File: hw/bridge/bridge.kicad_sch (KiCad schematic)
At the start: 37 parts, among them J1 USB_C_Receptacle_USB2.0_14P, J2 USB_C_Receptacle_USB2.0_14P, J3 DB9, U1 CH340E, U2 MAX485E, U3 74LVC2G240

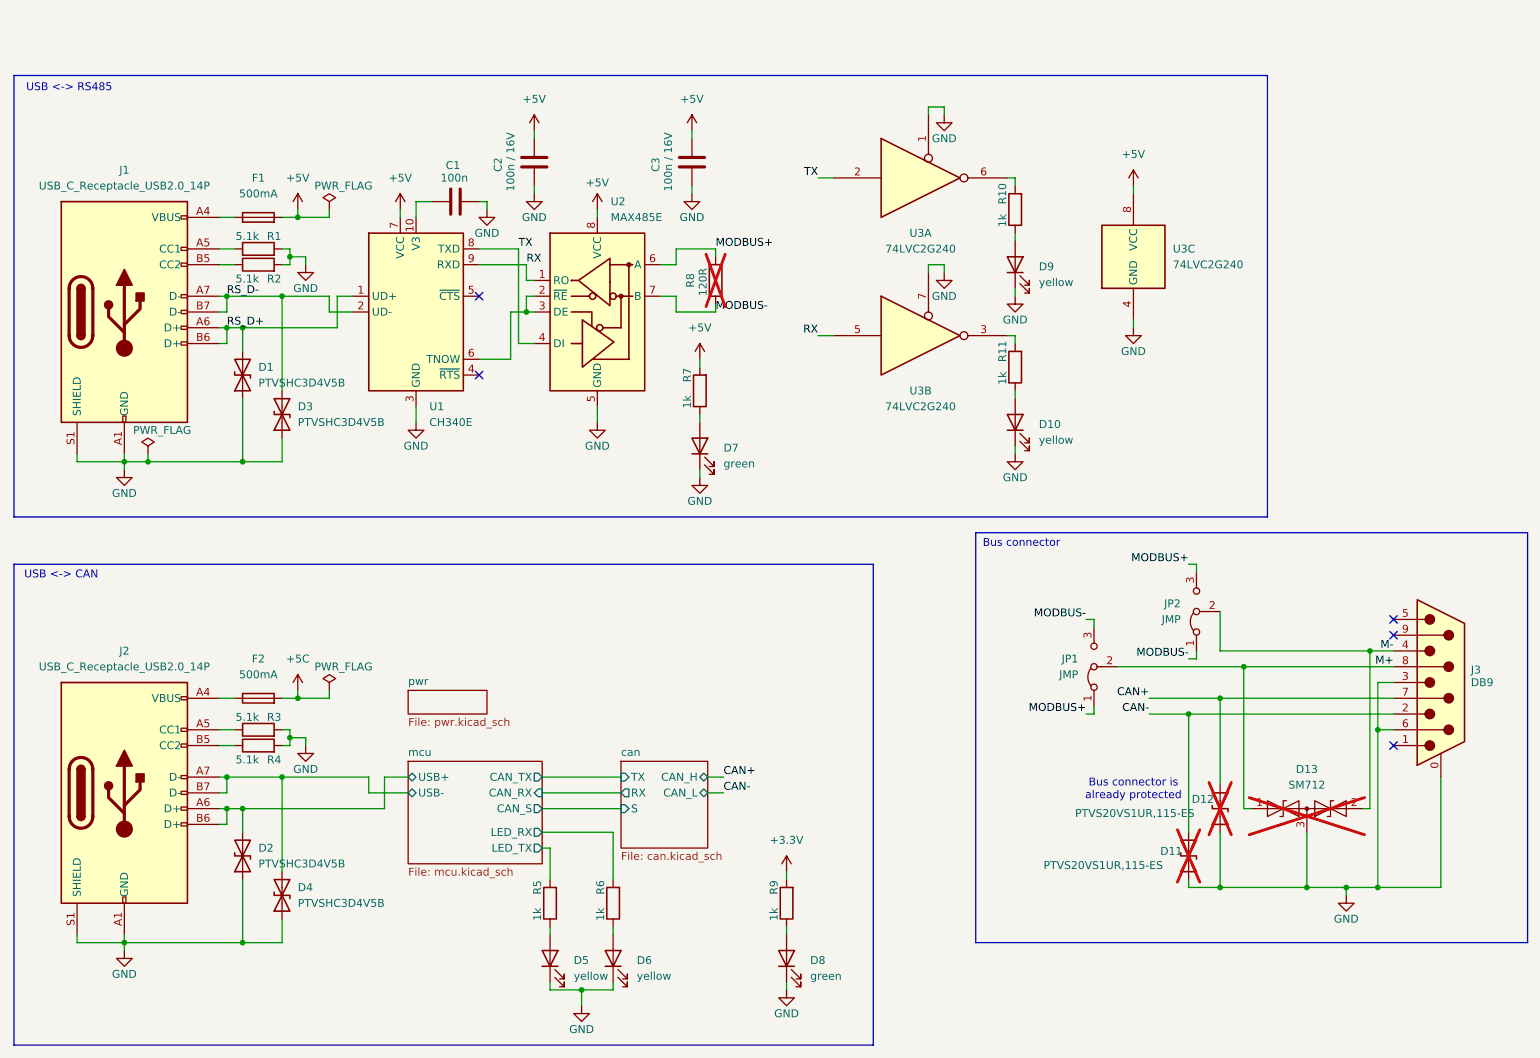
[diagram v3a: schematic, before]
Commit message: Redesign the PCB, remove DNP components
Signed-off-by: Mateusz Pająk <22417805+Tai-Min@users.noreply.github.com>
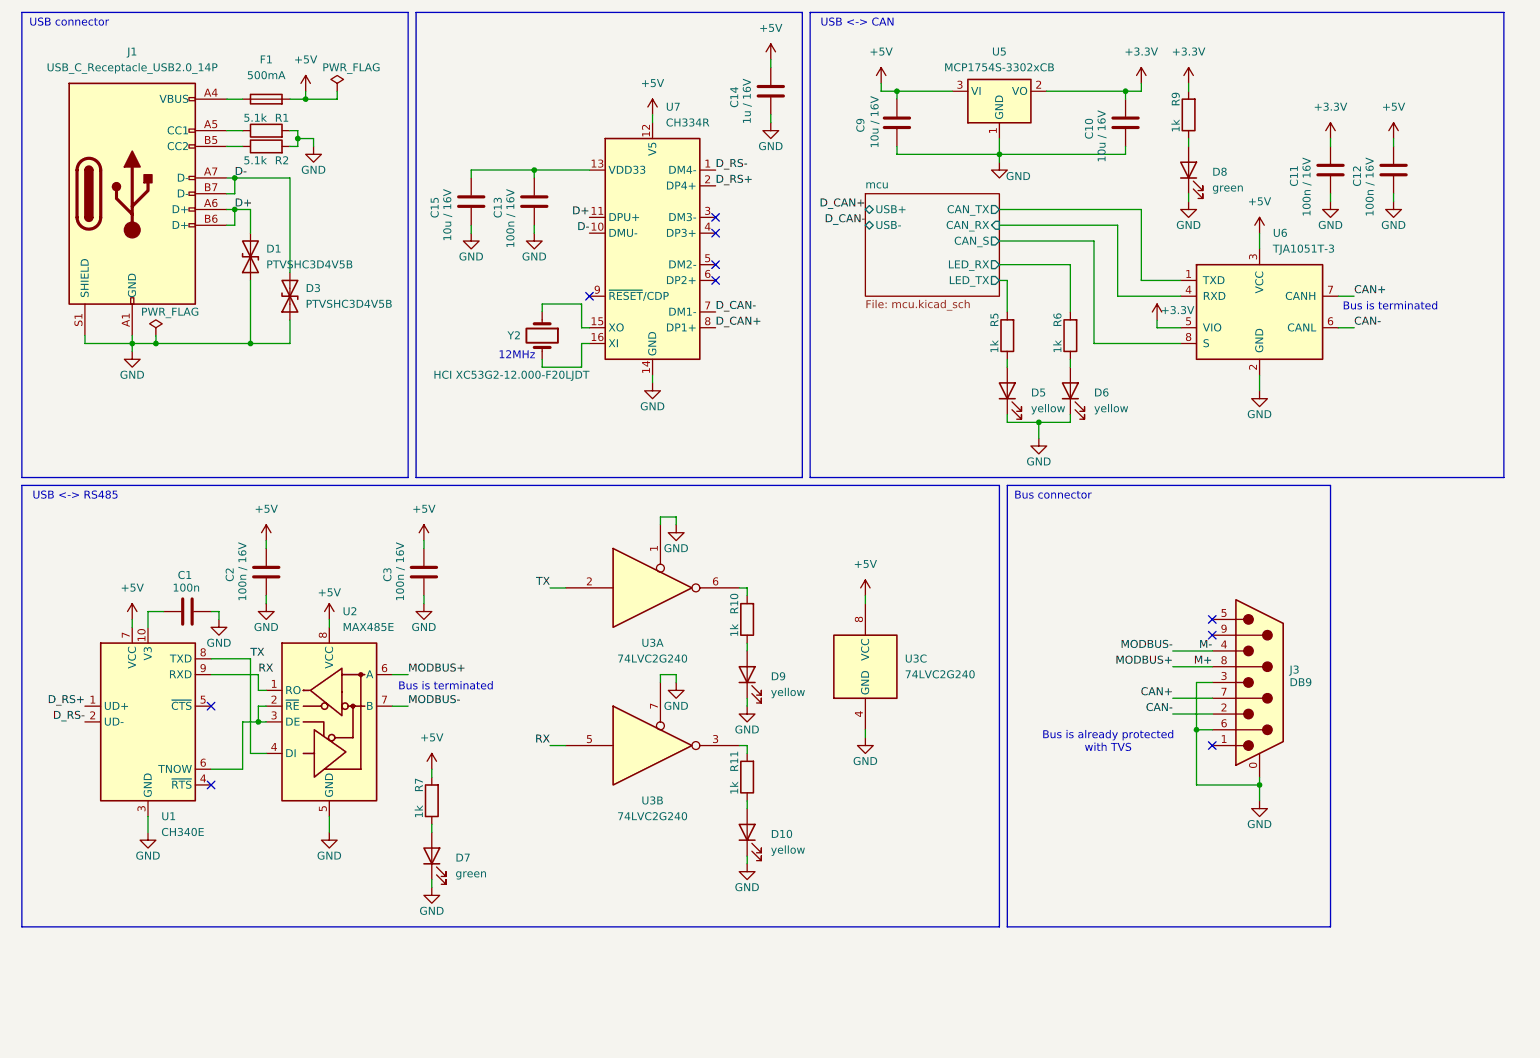
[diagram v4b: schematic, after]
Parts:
- removed D11, D12: PTVS20VS1UR,115-ES, Diode_SMD:D_SOD-123F, symbol Device:D_TVS
- removed D13: SM712, Package_TO_SOT_SMD:SOT-23, symbol Diode:SM712_SOT23
- removed D2, D4: PTVSHC3D4V5B, Diode_SMD:D_SOD-323, symbol Device:D_TVS
- removed F2: 500mA, Fuse:Fuse_1206_3216Metric, symbol Device:Fuse
- removed J2: USB_C_Receptacle_USB2.0_14P, Connector_USB:USB_C_Receptacle_Amphenol_12401610E4-2A_CircularHoles, symbol Connector:USB_C_Receptacle_USB2.0_14P
- removed JP1, JP2: JMP, Jumper:SolderJumper-3_P1.3mm_Bridged2Bar12_RoundedPad1.0x1.5mm, symbol Jumper:Jumper_3_Bridged12
- removed R3, R4: 5.1k, Resistor_SMD:R_1206_3216Metric, symbol Device:R
- removed R8: 120R, Resistor_SMD:R_1206_3216Metric, symbol Device:R
- added C10, C15, C9: 10u / 16V, Capacitor_SMD:C_0603_1608Metric, symbol Device:C
- added C11, C12, C13: 100n / 16V, Capacitor_SMD:C_0603_1608Metric, symbol Device:C
- added C14: 1u / 16V, Capacitor_SMD:C_0603_1608Metric, symbol Device:C
- added U5: MCP1754S-3302xCB, Package_TO_SOT_SMD:SOT-23, symbol Regulator_Linear:MCP1754S-3302xCB
- added U6: TJA1051T-3, Package_SO:SOIC-8_3.9x4.9mm_P1.27mm, symbol Interface_CAN_LIN:TJA1051T-3
- added U7: CH334R, Package_SO:QSOP-16_3.9x4.9mm_P0.635mm, symbol Interface_USB:CH334R
- added Y2: HCI XC53G2-12.000-F20LJDT, Crystal:Crystal_SMD_5032-2Pin_5.0x3.2mm, symbol Device:Crystal
- C1, C2, C3: footprint Capacitor_SMD:C_1206_3216Metric -> Capacitor_SMD:C_0603_1608Metric
- D10, D5, D6, D7, D8, D9: footprint LED_SMD:LED_1206_3216Metric -> LED_SMD:LED_0603_1608Metric
- F1: footprint Fuse:Fuse_1206_3216Metric -> Fuse:Fuse_0603_1608Metric
- R1, R10, R11, R2, R5, R6, R7, R9: footprint Resistor_SMD:R_1206_3216Metric -> Resistor_SMD:R_0603_1608Metric
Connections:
- net MODBUS+ is gone; now on net M+: U2.6 (A)
- net MODBUS- is gone; now on net M-: U2.7 (B)
- net +3.3V: now also C10.2, C11.2, U5.2 (VO), U6.5 (VIO)
- net +5V: now also C12.2, C14.2, C9.2, U5.3 (VI), U6.3 (VCC), U7.12 (V5)
- net CAN+: now also U6.7 (CANH)
- net CAN-: now also U6.6 (CANL)
- net GND: now also C10.1, C11.1, C12.1, C13.1, C14.1, C15.1, C9.1, U5.1 (GND), U6.2 (GND), U7.14 (GND)
- net RS_D+ renamed D+
- net D+: now also U7.11 (DPU+); no longer U1.1 (UD+)
- net RS_D- renamed D-
- net D-: now also U7.10 (DMU-); no longer U1.2 (UD-)
- new net: C13.2, C15.2, U7.13 (VDD33)
- new net: U7.15 (XO), Y2.1
- new net: U7.16 (XI), Y2.2
- new net D_CAN+: U7.8 (DP1+)
- new net D_CAN-: U7.7 (DM1-)
- new net D_RS+: U1.1 (UD+), U7.2 (DP4+)
- new net D_RS-: U1.2 (UD-), U7.1 (DM4-)
- new net mcu/CAN_RX: U6.4 (RXD)
- new net mcu/CAN_S: U6.8 (S)
- new net mcu/CAN_TX: U6.1 (TXD)
- no-connect marks 5 -> 10
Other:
- removed sheet can
- removed sheet pwr
- note added: "12MHz"
- note added: "Bus is already protected with TVS"
- note added: "Bus is terminated"
- note added: "USB connector"
- note removed: "Bus connector is already protected"
- moved on the sheet: C1, C2, C3, D1, D10, D3, D5, D6, D7, D8, D9, F1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

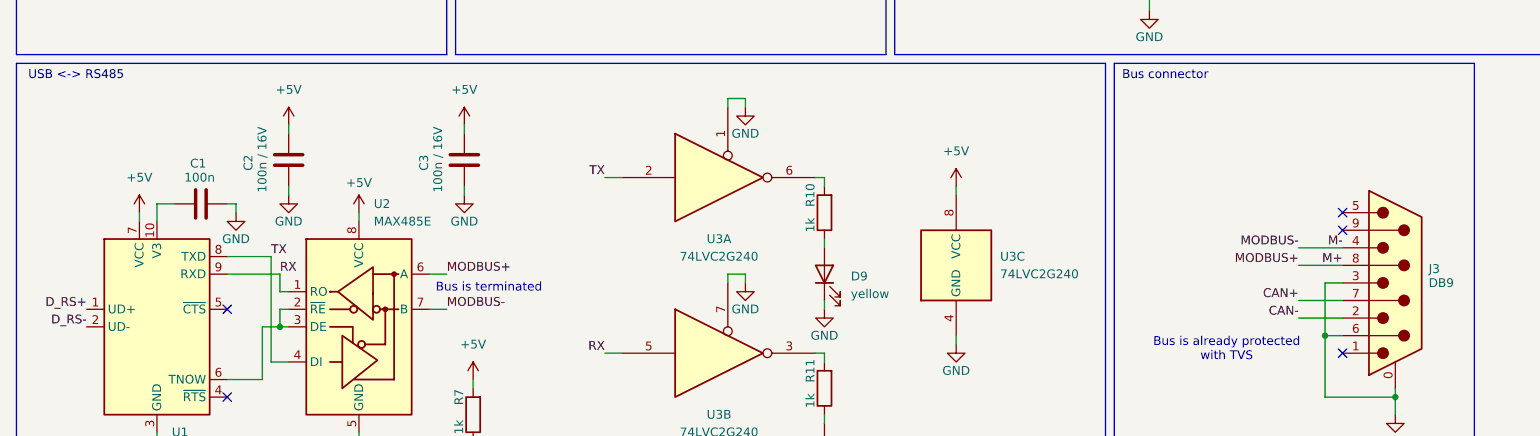
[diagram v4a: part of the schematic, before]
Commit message: Add datasheets, add BOM links
Signed-off-by: Mateusz Pająk <22417805+Tai-Min@users.noreply.github.com>
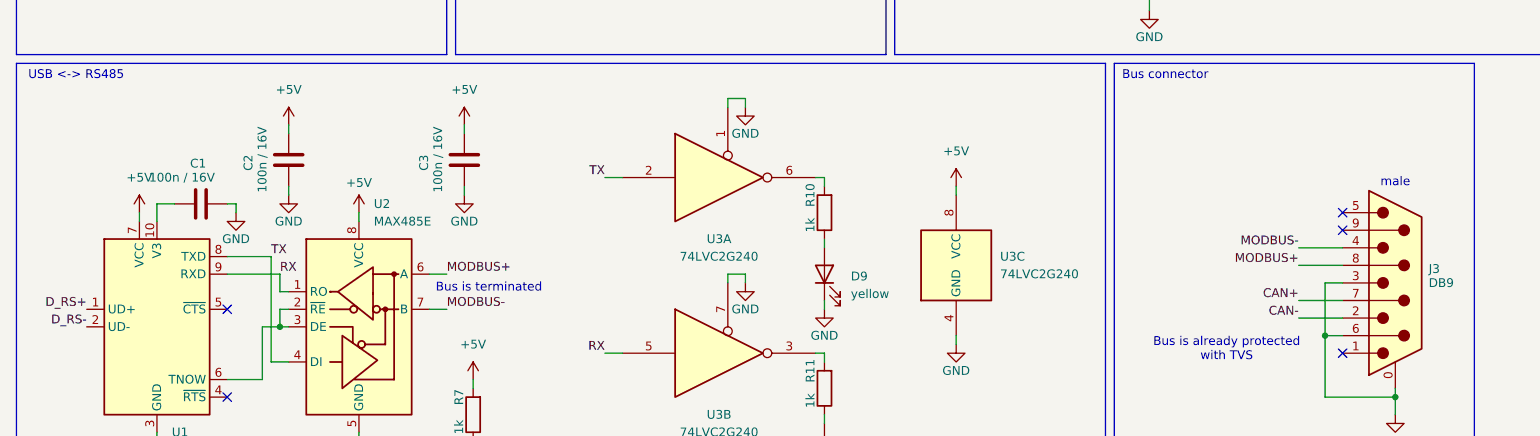
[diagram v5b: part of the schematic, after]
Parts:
- C1: value 100n -> 100n / 16V; LCSC (none) -> https://www.lcsc.com/product-detail/C66501.html
- C10, C15, C9: LCSC (none) -> https://www.lcsc.com/product-detail/C92487.html
- C11, C12, C13, C2, C3: LCSC (none) -> https://www.lcsc.com/product-detail/C66501.html
- C14: LCSC (none) -> https://www.lcsc.com/product-detail/C1592.html
- D1, D3: LCSC (none) -> https://www.lcsc.com/product-detail/C110752.html?s_z=n_PTVS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
- D10, D5, D6, D9: LCSC (none) -> https://www.lcsc.com/product-detail/C72038.html
- D7, D8: LCSC (none) -> https://www.lcsc.com/product-detail/C22371297.html
- F1: LCSC (none) -> https://www.lcsc.com/product-detail/C41380225.html
- J1: LCSC (none) -> https://www.lcsc.com/product-detail/C5119948.html?s_z=n_124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
- J3: LCSC (none) -> https://www.lcsc.com/product-detail/C19077344.html?s_z=n_ds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
- R1, R2: LCSC (none) -> https://www.lcsc.com/product-detail/C2907044.html
- R10, R11, R5, R6, R7, R9: LCSC (none) -> https://www.lcsc.com/product-detail/C22548.html
- U1: LCSC (none) -> https://www.lcsc.com/product-detail/C99652.html?s_z=n_ch340e
- U2: LCSC (none) -> https://www.lcsc.com/product-detail/C481667.html?s_z=n_max4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
- U3: LCSC (none) -> https://www.lcsc.com/product-detail/C730238.html?s_z=n_74LV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
- U5: LCSC (none) -> https://www.lcsc.com/product-detail/C625392.html?s_z=n_MCP1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
- U6: LCSC (none) -> https://www.lcsc.com/product-detail/C51954344.html?s_z=n_TJ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
- U7: LCSC (none) -> https://www.lcsc.com/product-detail/C4154405.html?s_z=n_ch3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
- Y2: LCSC (none) -> https://www.lcsc.com/product-detail/C2842275.html?s_z=n_HCI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
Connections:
- net M+ renamed MODBUS+
- net M- renamed MODBUS-
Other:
- note added: "male"

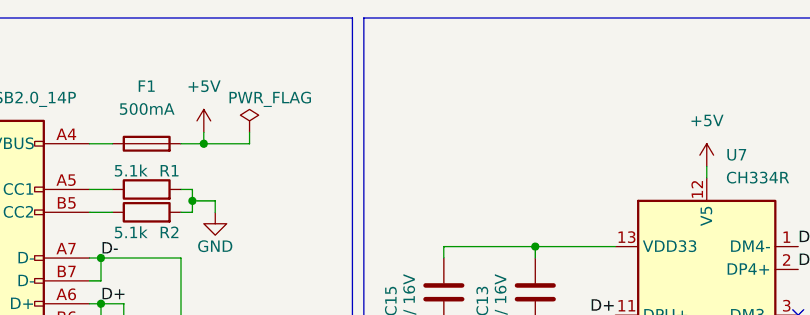
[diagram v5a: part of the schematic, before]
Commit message: Fix missing schematic header
Signed-off-by: Mateusz Pająk <22417805+Tai-Min@users.noreply.github.com>
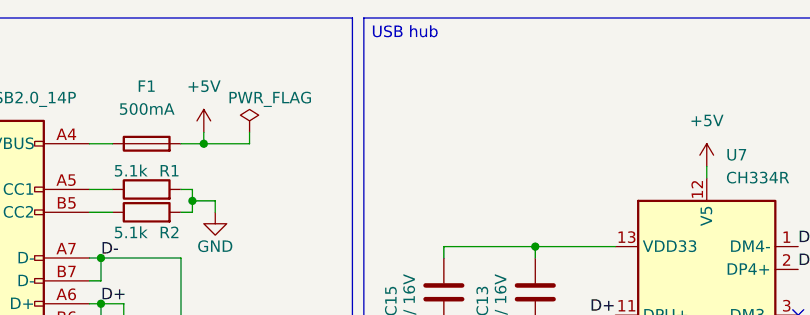
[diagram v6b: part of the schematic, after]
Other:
- note added: "USB hub"
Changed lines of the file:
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@@
+		)
+	)
+	(text "USB hub"
+		(exclude_from_sim no)
+		(at 97.282 15.748 0)
+		(effects
+			(font
+				(size 1.27 1.27)
+			)
 		)
 	)

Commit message: Minor fixes
Signed-off-by: Mateusz Pająk <22417805+Tai-Min@users.noreply.github.com>
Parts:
- removed U3: 74LVC2G240, Package_SO:TSSOP-8_3x3mm_P0.65mm, symbol 74xGxx:74LVC2G240
- added C4: 1u, Capacitor_SMD:C_0603_1608Metric, symbol Device:C
- added R12, R13, R14, R15: 0, Resistor_SMD:R_0603_1608Metric, symbol Device:R
- added R3, R4: 10k, Resistor_SMD:R_0603_1608Metric, symbol Device:R
- added U4: 74LVC2G04, Package_TO_SOT_SMD:SOT-23-6, symbol 74xGxx:74LVC2G04
- C1: renamed from C2; value 100n / 16V -> 100n
- C10: renamed from C11; value 100n / 16V -> 100n
- C11: renamed from C12; value 100n / 16V -> 100n
- C2: renamed from C1; value 100n / 16V -> 100n
- C3: value 100n / 16V -> 100n
- C5: renamed from C15; value 10u / 16V -> 10u
- C6: renamed from C13; value 100n / 16V -> 100n
- C7: renamed from C14; value 1u / 16V -> 1u
- C8: renamed from C9; value 10u / 16V -> 10u
- C9: renamed from C10; value 10u / 16V -> 10u
- J2: renamed from J3; value DB9 -> DE9
- Y1: renamed from Y2; Freq (none) -> 12MHz
- renumbered D3 to D2, D9 to D3, D10 to D4, D7 to D5, D5 to D6, D6 to D7, R9 to R10, R10 to R5, R11 to R6, R5 to R8, R6 to R9, U7 to U3
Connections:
- net +3.3V: now also R4.2
- net +5V: now also R3.1, U4.5 (VCC); no longer C3.2
- net CAN+: now also R12.1; no longer U6.7 (CANH)
- net CAN-: now also R13.1; no longer U6.6 (CANL)
- net GND: now also C4.1, U4.2 (GND)
- net MODBUS+: now also R14.1; no longer U2.6 (A)
- net MODBUS-: now also R15.1; no longer U2.7 (B)
- net RX: now also R3.2, U4.3
- net TX: now also U4.1
- net at R6.2: now also U4.4
- net at U3.9 (~{RESET}/CDP): now also R4.1
- net VUSB: now reaches F1.1, J1.A4 (VBUS), J1.A9 (VBUS), J1.B4 (VBUS), J1.B9 (VBUS)
- net VUSB: now also C3.2, C4.2
- net at R5.2: now also U4.6
- new net: R15.2, U2.7 (B)
- new net: R14.2, U2.6 (A)
- new net: R12.2, U6.7 (CANH)
- new net: R13.2, U6.6 (CANL)
- no-connect marks 10 -> 9
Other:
- note added: "Optional spots for RC filter resistors for noise filtration"
- note added: "Terminators and bus protection are included in bus_connector PCB"
- note removed: "12MHz"
- note removed: "Bus is already protected with TVS"
- note removed: "Bus is terminated"
- moved on the sheet: C1, C2, D1, D2, D3, D4, D5, F1, J1, R1, R2, R5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
